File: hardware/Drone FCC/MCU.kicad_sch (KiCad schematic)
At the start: 45 parts, among them SW101 SW RESET, U101 STM32F746ZGTx, Y101 12MHz, Y102 32.768kHz

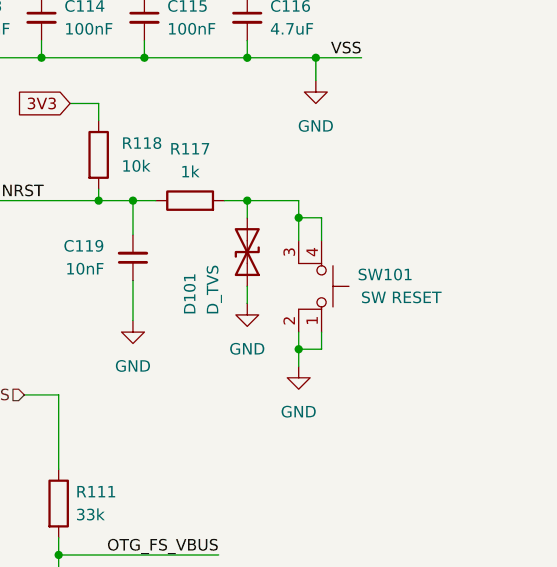
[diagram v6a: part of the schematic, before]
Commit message: changed sw with smaller sw
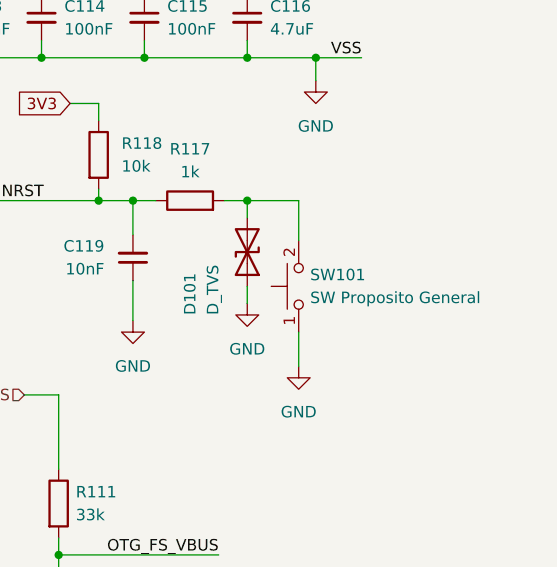
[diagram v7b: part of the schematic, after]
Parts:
- removed SW101: SW RESET, TL3305AF160QG:SW_TL3305AF160QG, symbol Switch:SW_MEC_5E
- added SW101: SW Proposito General, 434121043816:434121043816, symbol 434121043816:SW_SPST
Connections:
- net GND: now also SW101.1 (A)
- net at D101.2 (A2), R117.2: now also SW101.2 (B)
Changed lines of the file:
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@@
   (junction (at 247.65 40.64) (diameter 0) (color 0 0 0 0)
   )
-  (junction (at 276.225 81.915) (diameter 0) (color 0 0 0 0)
-  )
   (junction (at 259.08 49.53) (diameter 0) (color 0 0 0 0)
   )
@@
   )
   (junction (at 203.835 17.78) (diameter 0) (color 0 0 0 0)
-  )
-  (junction (at 276.225 67.31) (diameter 0) (color 0 0 0 0)
   )
   (junction (at 254 65.405) (diameter 0) (color 0 0 0 0)
@@
     (stroke (width 0) (type default) (color 0 0 0 0))
   )
-  (wire (pts (xy 276.225 65.405) (xy 276.225 67.31))
+  (wire (pts (xy 276.225 65.405) (xy 276.225 69.85))
     (stroke (width 0) (type default) (color 0 0 0 0))
   )
@@
     (stroke (width 0) (type default) (color 0 0 0 0))
   )
-  (wire (pts (xy 276.225 67.31) (xy 276.225 69.85))
-    (stroke (width 0) (type default) (color 0 0 0 0))
-  )
   (wire (pts (xy 137.16 45.72) (xy 137.16 32.385))
     (stroke (width 0) (type default) (color 0 0 0 0))
@@
     (stroke (width 0) (type default) (color 0 0 0 0))
   )
-  (wire (pts (xy 276.225 81.915) (xy 276.225 83.82))
-    (stroke (width 0) (type default) (color 0 0 0 0))
-  )
   (polyline (pts (xy 226.06 112.395) (xy 228.6 112.395))
     (stroke (width 0) (type default) (color 0 0 0 0))
@@
     (stroke (width 0) (type default) (color 0 0 0 0))
   )
-  (wire (pts (xy 276.225 80.01) (xy 276.225 81.915))
+  (wire (pts (xy 276.225 80.01) (xy 276.225 83.82))
     (stroke (width 0) (type default) (color 0 0 0 0))
   )
@@
     (stroke (width 0) (type default) (color 0 0 0 0))
   )
-  (wire (pts (xy 278.765 67.31) (xy 276.225 67.31))
-    (stroke (width 0) (type default) (color 0 0 0 0))
-  )
   (wire (pts (xy 156.845 156.21) (xy 172.085 156.21))
     (stroke (width 0) (type default) (color 0 0 0 0))
@@
     (stroke (width 0) (type default) (color 0 0 0 0))
   )
-  (wire (pts (xy 278.765 81.915) (xy 278.765 80.01))
-    (stroke (width 0) (type default) (color 0 0 0 0))
-  )
   (wire (pts (xy 154.94 129.54) (xy 168.275 129.54))
     (stroke (width 0) (type default) (color 0 0 0 0))
@@
     (stroke (width 0) (type default) (color 0 0 0 0))
   )
-  (wire (pts (xy 276.225 81.915) (xy 278.765 81.915))
-    (stroke (width 0) (type default) (color 0 0 0 0))
-  )
   (wire (pts (xy 26.67 101.6) (xy 43.18 101.6))
     (stroke (width 0) (type default) (color 0 0 0 0))
@@
   )
   (wire (pts (xy 227.33 38.1) (xy 236.22 38.1))
-    (stroke (width 0) (type default) (color 0 0 0 0))
-  )
-  (wire (pts (xy 278.765 69.85) (xy 278.765 67.31))
     (stroke (width 0) (type default) (color 0 0 0 0))
   )
@@
     (pin "2")
   )
-  (symbol (lib_id "Switch:SW_MEC_5E") (at 276.225 74.93 270) (mirror x) (unit 1)
-    (in_bom yes) (on_board yes)
-    (property "Reference" "SW101" (id 0) (at 288.925 73.66 90)
-      (effects (font (size 1.27 1.27)) (justify right))
-    )
-    (property "Value" "SW RESET" (id 1) (at 292.1 76.2 90)
-      (effects (font (size 1.27 1.27)) (justify right))
-    )
-    (property "Footprint" "TL3305AF160QG:SW_TL3305AF160QG" (id 2) (at 283.845 74.93 0)
-      (effects (font (size 1.27 1.27)) hide)
-    )
-    (property "Datasheet" "http://www.apem.com/int/index.php?controller=attachment&id_attachment=1371" (id 3) (at 283.845 74.93 0)
-      (effects (font (size 1.27 1.27)) hide)
-    )
-    (pin "1")
-    (pin "2")
-    (pin "3")
-    (pin "4")
-  )
   (symbol (lib_id "Device:D_TVS") (at 270.51 71.12 270) (mirror x) (unit 1)
     (in_bom yes) (on_board yes)
@@
     (pin "1")
   )
+  (symbol (lib_id "434121043816:SW_SPST") (at 276.225 74.93 90) (unit 1)
+    (in_bom yes) (on_board yes) (fields_autoplaced)
+    (property "Reference" "SW101" (id 0) (at 277.495 73.6599 90)
+      (effects (font (size 1.27 1.27)) (justify right))
+    )
+    (property "Value" "SW Proposito General" (id 1) (at 277.495 76.1999 90)
+      (effects (font (size 1.27 1.27)) (justify right))
+    )
+    (property "Footprint" "434121043816:434121043816" (id 2) (at 276.225 74.93 0)
+      (effects (font (size 1.27 1.27)) hide)
+    )
+    (property "Datasheet" "~" (id 3) (at 276.225 74.93 0)
+      (effects (font (size 1.27 1.27)) hide)
+    )
+    (pin "1")
+    (pin "2")
+  )
 )

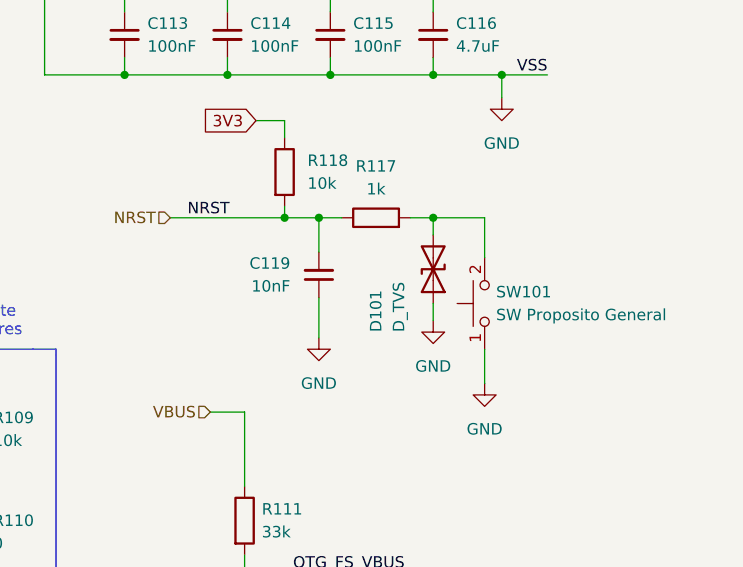
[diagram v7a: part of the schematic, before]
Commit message: removed all the TVS from the PCB and SCH
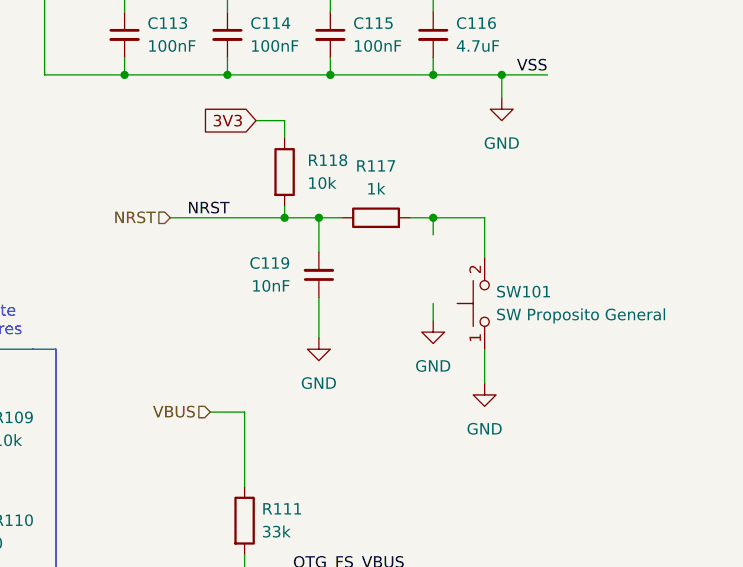
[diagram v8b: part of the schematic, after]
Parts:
- removed D101: D_TVS, Diode_SMD:D_0402_1005Metric_Pad0.77x0.64mm_HandSolder, symbol Device:D_TVS
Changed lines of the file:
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@@
-    (pin "2")
-  )
-  (symbol (lib_id "Device:D_TVS") (at 270.51 71.12 270) (mirror x) (unit 1)
-    (in_bom yes) (on_board yes)
-    (property "Reference" "D101" (id 0) (at 264.16 78.105 0)
-      (effects (font (size 1.27 1.27)) (justify left))
-    )
-    (property "Value" "D_TVS" (id 1) (at 266.7 78.105 0)
-      (effects (font (size 1.27 1.27)) (justify left))
-    )
-    (property "Footprint" "Diode_SMD:D_0402_1005Metric_Pad0.77x0.64mm_HandSolder" (id 2) (at 270.51 71.12 0)
-      (effects (font (size 1.27 1.27)) hide)
-    )
-    (property "Datasheet" "~" (id 3) (at 270.51 71.12 0)
-      (effects (font (size 1.27 1.27)) hide)
-    )
-    (pin "1")
     (pin "2")
   )
